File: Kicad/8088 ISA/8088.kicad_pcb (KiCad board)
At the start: 2 copper layers, 132 x 73.9 mm, 28 parts, among them J1 Conn_02x08_Counter_Clockwise, J9 Bus_ISA_8bit, U1 8284, U2 74LS573, U3 74LS573, U4 74LS245, U5 8088, U6 8259, U7 8253, U8 74LS257, Y1 Crystal

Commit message: Updated Kicad files
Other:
- board text added: "EMM COMPUTERS 8088/V20 PROCESSOR, 8259, 8253 Copyright (C) 2022 EMM www.homebrew8088.com"
- board text removed: "EMM COMPUTERS 8088/V20 PROCESSOR, 8259, 8253 Copyright (C) 2021 EMM www.homebrew8088.com"

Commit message: update 8088 card
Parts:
- moved C2 45.8 mm to (111.5, 66.3)
- moved C3 45.8 mm to (109.0, 112.1)
- moved C8 39.9 mm to (171.8, 85.8), turned to 0 degrees
- moved C5 27.9 mm to (136.9, 66.3)
- moved C6 20.7 mm to (164.8, 66.3), turned to 270 degrees
- renumbered R2 to R1, R4 to R2, R5 to R4, R1 to R5, U5 to U1, U3 to U2, U2 to U3, U8 to U5, U1 to U6, U6 to U7, U7 to U8
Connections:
- net /PCLK88 renamed Net-(J1-Pad7)

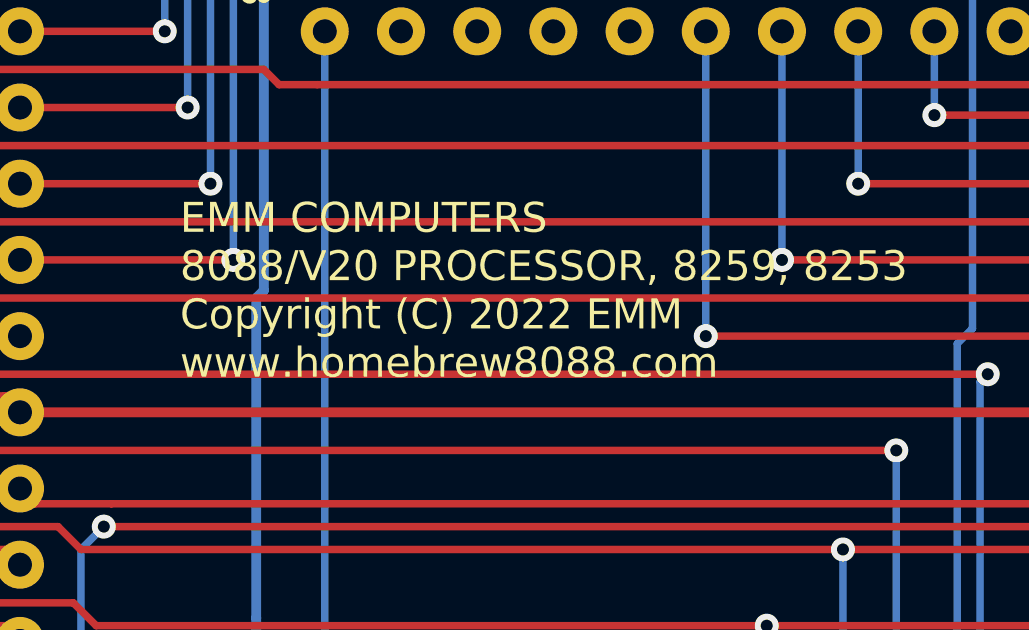
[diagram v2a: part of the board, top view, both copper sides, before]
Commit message: updated DMA
Added DMA controller to main board.
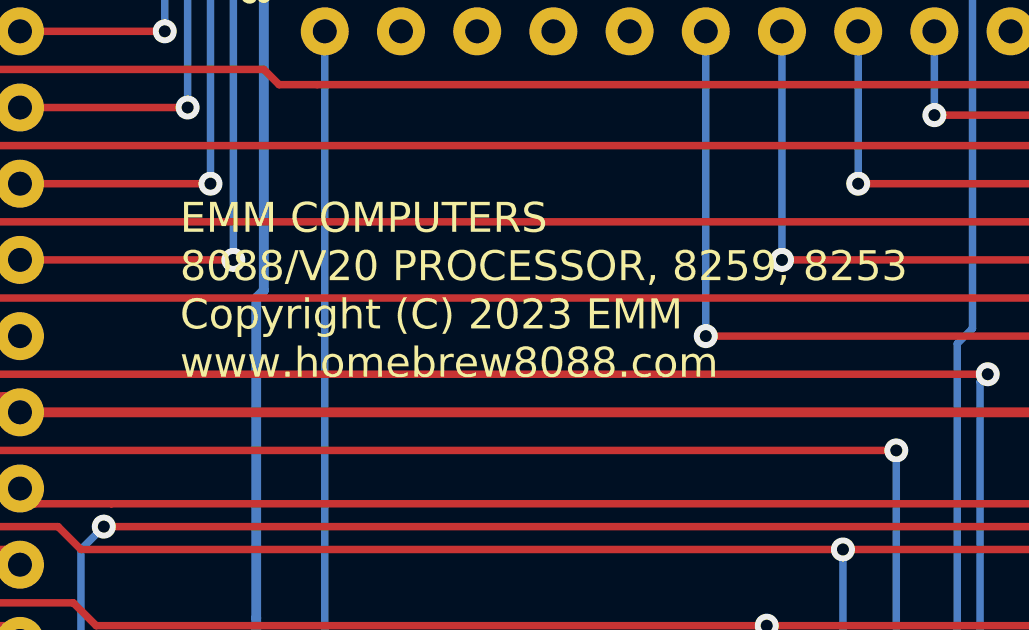
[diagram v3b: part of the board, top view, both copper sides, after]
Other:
- board text added: "EMM COMPUTERS 8088/V20 PROCESSOR, 8259, 8253 Copyright (C) 2023 EMM www.homebrew8088.com"
- board text removed: "EMM COMPUTERS 8088/V20 PROCESSOR, 8259, 8253 Copyright (C) 2022 EMM www.homebrew8088.com"

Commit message: Updated Gerber's
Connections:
- U8 pad 13: Net-(U8-Pad13) -> /DRQ0
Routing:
- net /DRQ0: track 0.00 -> 123.5 mm, vias 0 -> 3
